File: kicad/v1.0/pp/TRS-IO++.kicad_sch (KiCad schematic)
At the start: 86 parts, among them J1 Conn_02x06_Odd_Even, J12 USB_B_Micro, J13 UART, J2 Interface Connector, J3 TRS-80 M3 Edge Connector, J5 Conn_02x06_Odd_Even, J6 Cassette Output, J7 HDMI, J8 Programmer, Q3 2N7002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

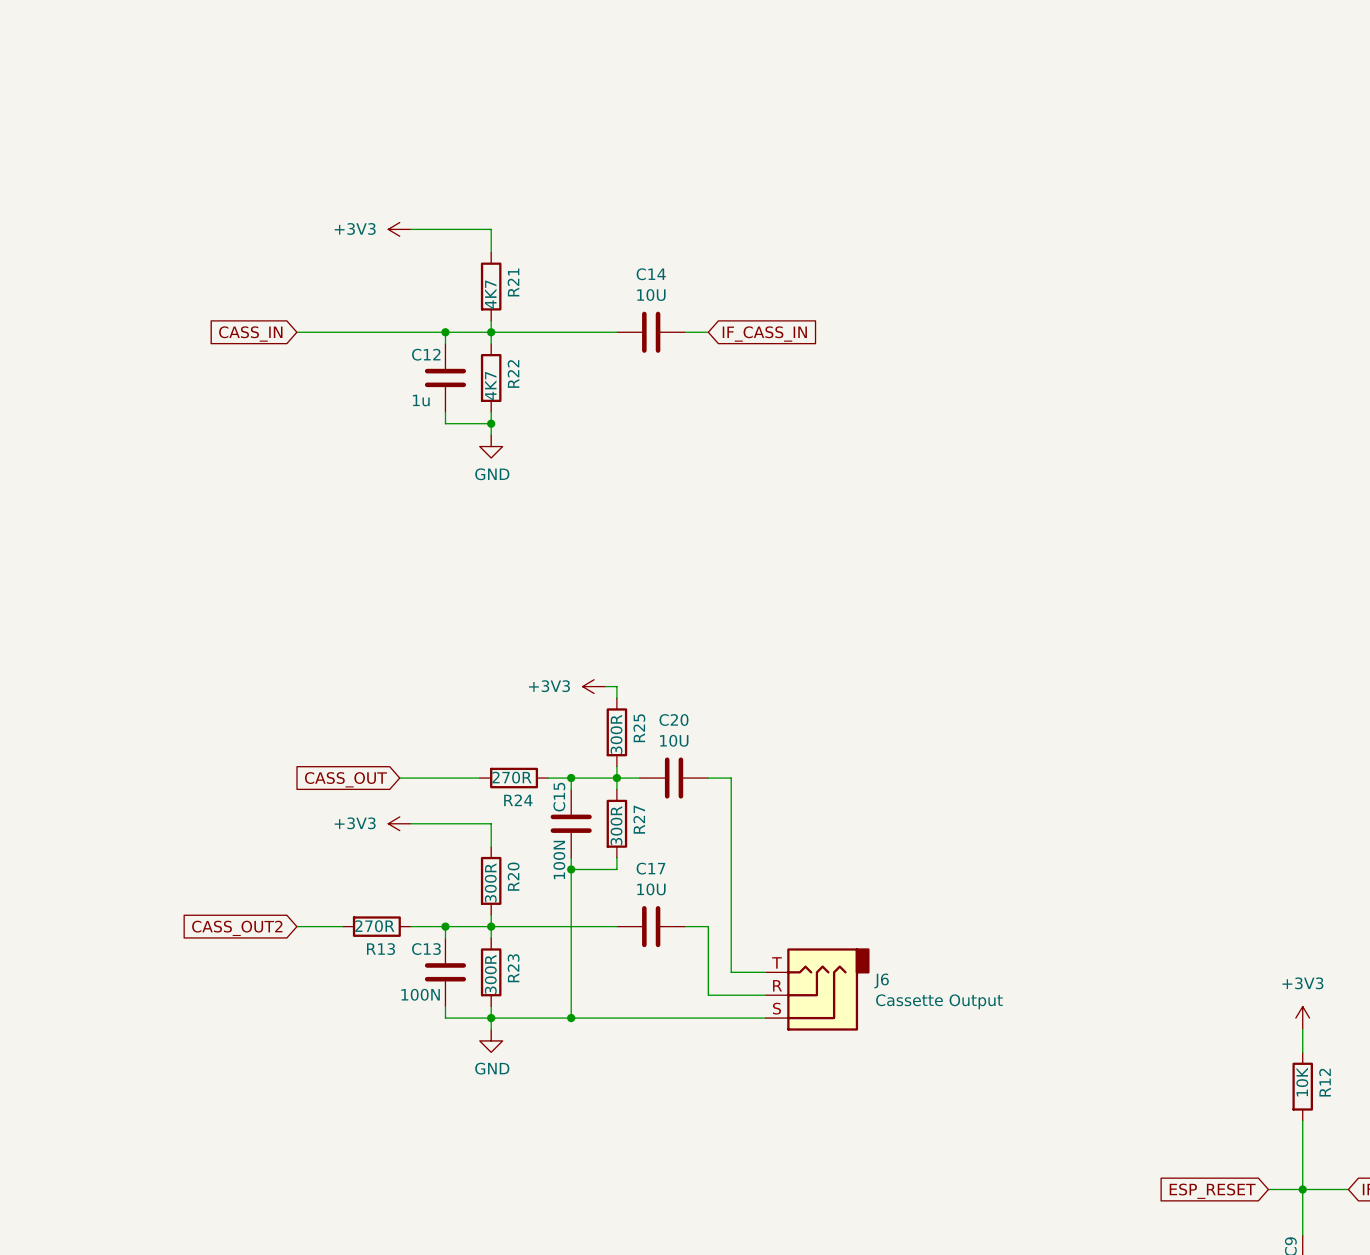
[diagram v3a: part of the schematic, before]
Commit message: Converted cassette to mono in/out.  Added audio amp.
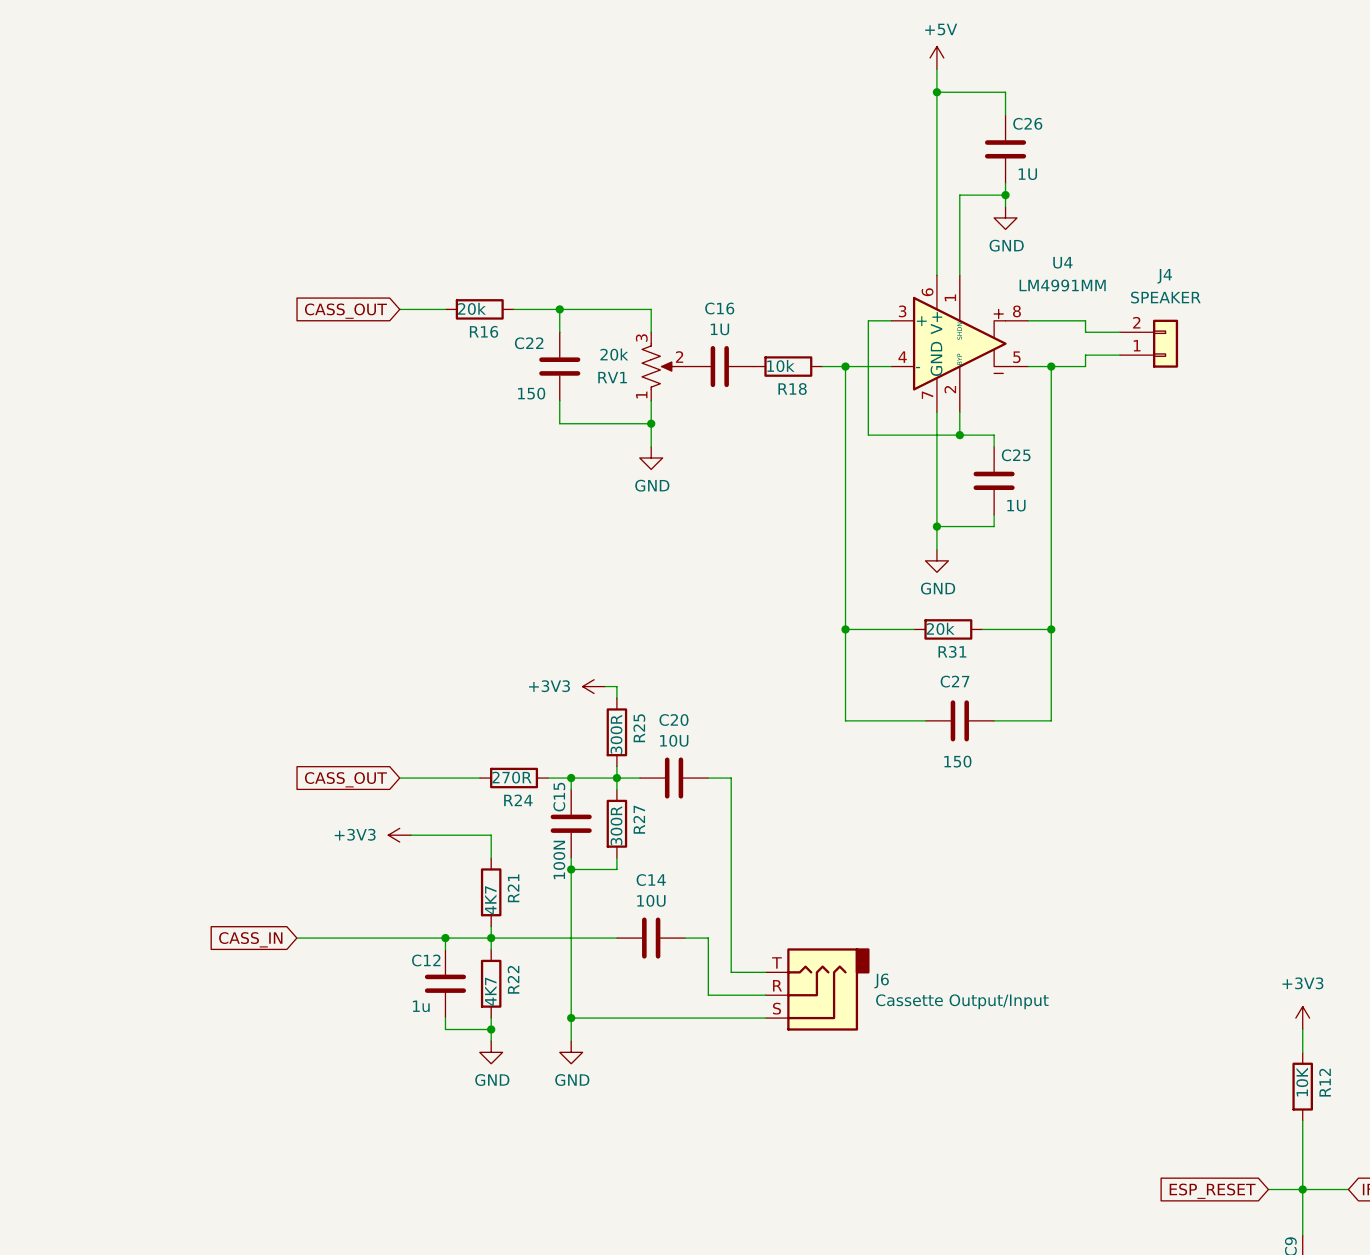
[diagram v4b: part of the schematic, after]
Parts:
- removed C13: 100N, Capacitor_SMD:C_0805_2012Metric_Pad1.18x1.45mm_HandSolder, symbol Device:C
- removed C17: 10U, Capacitor_SMD:C_1206_3216Metric_Pad1.33x1.80mm_HandSolder, symbol Device:C
- removed R13: 270R, Resistor_SMD:R_0805_2012Metric_Pad1.20x1.40mm_HandSolder, symbol Device:R
- removed R20, R23: 300R, Resistor_SMD:R_0805_2012Metric_Pad1.20x1.40mm_HandSolder, symbol Device:R
- added C16, C25, C26: 1U, Capacitor_SMD:C_0805_2012Metric_Pad1.18x1.45mm_HandSolder, symbol Device:C
- added C22, C27: 150, Capacitor_SMD:C_0805_2012Metric_Pad1.18x1.45mm_HandSolder, symbol Device:C
- added J4: SPEAKER, Connector_PinHeader_2.54mm:PinHeader_1x02_P2.54mm_Vertical, symbol Connector_Generic:Conn_01x02
- added R16, R31: 20k, Resistor_SMD:R_0805_2012Metric_Pad1.20x1.40mm_HandSolder, symbol Device:R
- added R18: 10k, Resistor_SMD:R_0805_2012Metric_Pad1.20x1.40mm_HandSolder, symbol Device:R
- added RV1: 20k, Potentiometer_SMD:Potentiometer_Bourns_TC33X_Vertical, symbol Device:R_Potentiometer_US
- added U4: LM4991MM, Package_SO:SOIC-8_3.9x4.9mm_P1.27mm, symbol Amplifier_Audio:LM4990MM
- J6: value Cassette Output -> Cassette Output/Input
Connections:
- net +5V: now also C26.1, U4.6 (V+)
- net CASS_OUT: now also R16.2
- net GND: now also C22.2, C25.2, C26.2, RV1.1, U4.1 (SHDN), U4.7 (GND)
- net IF_CASS_IN: no longer C14.1
- net at J6.R: now also C14.1
- new net: C25.1, U4.2 (BYP), U4.3 (+)
- new net: C27.2, R18.1, R31.2, U4.4 (-)
- new net: C27.1, J4.1 (Pin_1), R31.1, U4.5
- new net: J4.2 (Pin_2), U4.8
- new net: C16.2, RV1.2
- new net: C22.1, R16.1, RV1.3
- new net: C16.1, R18.2
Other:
- moved on the sheet: C12, C14, R21, R22

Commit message: First version of PCB (without HDMI)
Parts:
- removed D4, D5: LED, LED_SMD:LED_0805_2012Metric_Pad1.15x1.40mm_HandSolder, symbol Device:LED
- removed J12: USB_B_Micro, PocketTRS_Connectors:USBmicro-B, symbol MYLIB:USB_B_Micro
- removed J6: Cassette Output/Input, PocketTRS_Connectors:Jack_3.5mm_CUI_SJ1-3535NG_Horizontal_CircularHoles, symbol Connector:AudioJack3
- added J6: LED3, Connector_PinHeader_2.54mm:PinHeader_1x02_P2.54mm_Vertical, symbol Connector_Generic:Conn_01x02
- added J9: LED4, Connector_PinHeader_2.54mm:PinHeader_1x02_P2.54mm_Vertical, symbol Connector_Generic:Conn_01x02
- U4: LCSC (none) -> C2865568
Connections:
- net CD_SD: now also J2.15 (Pin_15); no longer J2.5 (Pin_5)
- net CS_SD: now also J2.14 (Pin_14); no longer J2.9 (Pin_9)
- net ESP_RESET: now also J2.9 (Pin_9); no longer J2.14 (Pin_14)
- net GND: now also J6.2 (Pin_2), J9.2 (Pin_2)
- net ID0: now also J2.10 (Pin_10); no longer J2.13 (Pin_13)
- net IF_BTN_TRSIO_STATUS: now also J2.12 (Pin_12); no longer J2.11 (Pin_11)
- net IF_CASS_IN: now also C14.1, J2.8 (Pin_8); no longer J2.12 (Pin_12)
- net IF_LED_BLUE: now also J2.5 (Pin_5); no longer J2.8 (Pin_8)
- net IF_LED_GREEN: now also J2.3 (Pin_3); no longer J2.6 (Pin_6)
- net IF_LED_RED: now also J2.7 (Pin_7); no longer J2.10 (Pin_10)
- net IF_RXD0: now also J2.6 (Pin_6); no longer J2.4 (Pin_4)
- net IF_SD_MISO: now also J2.11 (Pin_11); no longer J2.1 (Pin_1)
- net IF_SD_MOSI: now also J2.16 (Pin_16); no longer J2.7 (Pin_7)
- net IF_SD_SCK: now also J2.13 (Pin_13); no longer J2.3 (Pin_3)
- net IF_TXD0: now also J2.4 (Pin_4); no longer J2.2 (Pin_2)
- net IF_CASS_OUT: now reaches C20.1
- net IF_CASS_OUT: now also J2.2 (Pin_2)
- net at R39.2: now also J6.1 (Pin_1)
- net at R40.2: now also J9.1 (Pin_1)
- no-connect marks 11 -> 8
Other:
- moved on the sheet: D2, D3, R37, R38, R39, R40

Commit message: Converted HDMI connector to SMD.
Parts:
- J7: footprint Connector_PinHeader_1.27mm:PinHeader_2x05_P1.27mm_Vertical -> Connector_PinHeader_1.27mm:PinHeader_2x05_P1.27mm_Vertical_SMD
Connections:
- net CK+: now also J7.1 (Pin_1); no longer J7.7 (Pin_7)
- net CK-: now also J7.2 (Pin_2); no longer J7.8 (Pin_8)
- net D0+: now also J7.3 (Pin_3); no longer J7.5 (Pin_5)
- net D0-: now also J7.4 (Pin_4); no longer J7.6 (Pin_6)
- net D1+: now also J7.5 (Pin_5); no longer J7.3 (Pin_3)
- net D1-: now also J7.6 (Pin_6); no longer J7.4 (Pin_4)
- net D2+: now also J7.7 (Pin_7); no longer J7.1 (Pin_1)
- net D2-: now also J7.8 (Pin_8); no longer J7.2 (Pin_2)
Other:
- moved on the sheet: J7
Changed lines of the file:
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@@
 	)
 	(junction
+		(at 248.92 91.44)
+		(diameter 0)
+		(color 0 0 0 0)
+	)
+	(junction
 		(at 441.96 369.57)
 		(diameter 0)
@@
 	)
 	(junction
-		(at 248.92 91.44)
-		(diameter 0)
-		(color 0 0 0 0)
-	)
-	(junction
 		(at 238.76 349.25)
 		(diameter 0)
@@
 	(wire
 		(pts
-			(xy 279.4 83.82) (xy 271.78 83.82)
-		)
-		(stroke
-			(width 0)
-			(type default)
-		)
-	)
-	(wire
-		(pts
 			(xy 142.24 373.38) (xy 139.7 373.38)
 		)
@@
 	(wire
 		(pts
+			(xy 271.78 83.82) (xy 279.4 83.82)
+		)
+		(stroke
+			(width 0)
+			(type default)
+		)
+	)
+	(wire
+		(pts
 			(xy 276.86 48.26) (xy 280.67 48.26)
 		)
@@
 	(wire
 		(pts
-			(xy 299.72 88.9) (xy 292.1 88.9)
+			(xy 373.38 360.68) (xy 378.46 360.68)
 		)
 		(stroke
@@
 	(wire
 		(pts
-			(xy 373.38 360.68) (xy 378.46 360.68)
+			(xy 425.45 58.42) (xy 425.45 87.63)
 		)
 		(stroke
@@
 	(wire
 		(pts
-			(xy 425.45 58.42) (xy 425.45 87.63)
+			(xy 97.79 328.93) (xy 88.9 328.93)
 		)
 		(stroke
@@
 	(wire
 		(pts
-			(xy 97.79 328.93) (xy 88.9 328.93)
+			(xy 53.34 248.92) (xy 53.34 251.46)
 		)
 		(stroke
@@
 	(wire
 		(pts
-			(xy 53.34 248.92) (xy 53.34 251.46)
+			(xy 248.92 91.44) (xy 279.4 91.44)
 		)
 		(stroke
@@
 	(wire
 		(pts
+			(xy 276.86 81.28) (xy 279.4 81.28)
+		)
+		(stroke
+			(width 0)
+			(type default)
+		)
+	)
+	(wire
+		(pts
 			(xy 496.57 105.41) (xy 496.57 107.95)
 		)
@@
 	(wire
 		(pts
-			(xy 281.94 354.33) (xy 284.48 354.33)
+			(xy 292.1 88.9) (xy 299.72 88.9)
 		)
 		(stroke
@@
 	(wire
 		(pts
-			(xy 88.9 308.61) (xy 91.44 308.61)
+			(xy 281.94 354.33) (xy 284.48 354.33)
 		)
 		(stroke
@@
 	(wire
 		(pts
-			(xy 91.44 339.09) (xy 91.44 346.71)
+			(xy 88.9 308.61) (xy 91.44 308.61)
 		)
 		(stroke
@@
 	(wire
 		(pts
-			(xy 57.15 203.2) (xy 53.34 203.2)
+			(xy 91.44 339.09) (xy 91.44 346.71)
 		)
 		(stroke
@@
 	(wire
 		(pts
-			(xy 236.22 35.56) (xy 236.22 39.37)
+			(xy 57.15 203.2) (xy 53.34 203.2)
 		)
 		(stroke
@@
 	(wire
 		(pts
-			(xy 284.48 311.15) (xy 284.48 318.77)
+			(xy 236.22 35.56) (xy 236.22 39.37)
 		)
 		(stroke
@@
 	(wire
 		(pts
-			(xy 43.18 372.11) (xy 48.26 372.11)
+			(xy 284.48 311.15) (xy 284.48 318.77)
 		)
 		(stroke
@@
 	(wire
 		(pts
-			(xy 182.88 325.12) (xy 187.96 325.12)
+			(xy 43.18 372.11) (xy 48.26 372.11)
 		)
 		(stroke
@@
 	(wire
 		(pts
-			(xy 292.1 93.98) (xy 294.64 93.98)
+			(xy 182.88 325.12) (xy 187.96 325.12)
 		)
 		(stroke
@@
 	(wire
 		(pts
-			(xy 279.4 86.36) (xy 269.24 86.36)
-		)
-		(stroke
-			(width 0)
-			(type default)
-		)
-	)
-	(wire
-		(pts
 			(xy 53.34 220.98) (xy 53.34 223.52)
 		)
@@
 	(wire
 		(pts
-			(xy 299.72 86.36) (xy 292.1 86.36)
-		)
-		(stroke
-			(width 0)
-			(type default)
-		)
-	)
-	(wire
-		(pts
 			(xy 185.42 381) (xy 185.42 386.08)
 		)
@@
 	(wire
 		(pts
+			(xy 292.1 86.36) (xy 299.72 86.36)
+		)
+		(stroke
+			(width 0)
+			(type default)
+		)
+	)
+	(wire
+		(pts
 			(xy 137.16 347.98) (xy 142.24 347.98)
 		)
@@
 	(wire
 		(pts
-			(xy 292.1 91.44) (xy 297.18 91.44)
-		)
-		(stroke
-			(width 0)
-			(type default)
-		)
-	)
-	(wire
-		(pts
 			(xy 88.9 62.23) (xy 96.52 62.23)
 		)
@@
 	(wire
 		(pts
-			(xy 248.92 91.44) (xy 279.4 91.44)
-		)
-		(stroke
-			(width 0)
-			(type default)
-		)
-	)
-	(wire
-		(pts
 			(xy 358.14 250.19) (xy 358.14 255.27)
 		)
@@
 	(wire
 		(pts
+			(xy 269.24 86.36) (xy 279.4 86.36)
+		)
+		(stroke
+			(width 0)
+			(type default)
+		)
+	)
+	(wire
+		(pts
 			(xy 177.8 148.59) (xy 185.42 148.59)
 		)
@@
 	(wire
 		(pts
+			(xy 294.64 81.28) (xy 294.64 105.41)
+		)
+		(stroke
+			(width 0)
+			(type default)
+		)
+	)
+	(wire
+		(pts
 			(xy 505.46 170.18) (xy 514.35 170.18)
 		)
@@
 	(wire
 		(pts
+			(xy 266.7 88.9) (xy 279.4 88.9)
+		)
+		(stroke
+			(width 0)
+			(type default)
+		)
+	)
+	(wire
+		(pts
 			(xy 229.87 35.56) (xy 229.87 39.37)
 		)
@@
 	(wire
 		(pts
-			(xy 279.4 88.9) (xy 266.7 88.9)
-		)
-		(stroke
-			(width 0)
-			(type default)
-		)
-	)
-	(wire
-		(pts
 			(xy 254 160.02) (xy 259.08 160.02)
 		)
@@
 	(wire
 		(pts
-			(xy 294.64 93.98) (xy 294.64 105.41)
-		)
-		(stroke
-			(width 0)
-			(type default)
-		)
-	)
-	(wire
-		(pts
 			(xy 88.9 334.01) (xy 93.98 334.01)
 		)
@@
 	(wire
 		(pts
+			(xy 292.1 81.28) (xy 294.64 81.28)
+		)
+		(stroke
+			(width 0)
+			(type default)
+		)
+	)
+	(wire
+		(pts
 			(xy 393.7 125.73) (xy 389.89 125.73)
 		)
@@
 	(wire
 		(pts
-			(xy 276.86 93.98) (xy 279.4 93.98)
+			(xy 284.48 341.63) (xy 284.48 346.71)
 		)
 		(stroke
@@
 	(wire
 		(pts
-			(xy 284.48 341.63) (xy 284.48 346.71)
+			(xy 97.79 326.39) (xy 97.79 328.93)
 		)
 		(stroke
@@
 	(wire
 		(pts
-			(xy 97.79 326.39) (xy 97.79 328.93)
+			(xy 260.35 217.17) (xy 265.43 217.17)
 		)
 		(stroke
@@
 	(wire
 		(pts
-			(xy 260.35 217.17) (xy 265.43 217.17)
+			(xy 69.85 205.74) (xy 74.93 205.74)
 		)
 		(stroke
@@
 	(wire
 		(pts
-			(xy 69.85 205.74) (xy 74.93 205.74)
+			(xy 292.1 83.82) (xy 297.18 83.82)
 		)
 		(stroke
@@
 	(wire
 		(pts
-			(xy 292.1 83.82) (xy 297.18 83.82)
+			(xy 292.1 91.44) (xy 297.18 91.44)
 		)
 		(stroke
@@
 	(wire
 		(pts
-			(xy 276.86 48.26) (xy 276.86 93.98)
+			(xy 276.86 48.26) (xy 276.86 81.28)
 		)
 		(stroke
@@
 	(symbol
 		(lib_id "Connector_Generic:Conn_02x05_Odd_Even")
-		(at 284.48 88.9 0)
+		(at 284.48 86.36 0)
+		(mirror x)
 		(unit 1)
 		(exclude_from_sim no)
@@
 		(on_board yes)
 		(dnp no)
-		(fields_autoplaced yes)
 		(property "Reference" "J7"
-			(at 285.75 77.47 0)
+			(at 285.75 97.79 0)
 			(effects
 				(font
@@
 		)
 		(property "Value" "HDMI"
-			(at 285.75 80.01 0)
+			(at 285.75 95.25 0)
 			(effects
 				(font
@@
 			)
 		)
-		(property "Footprint" "Connector_PinHeader_1.27mm:PinHeader_2x05_P1.27mm_Vertical"
-			(at 284.48 88.9 0)
+		(property "Footprint" "Connector_PinHeader_1.27mm:PinHeader_2x05_P1.27mm_Vertical_SMD"
+			(at 284.48 86.36 0)
 			(effects
 				(font
@@
 		)
 		(property "Datasheet" "~"
-			(at 284.48 88.9 0)
+			(at 284.48 86.36 0)
 			(effects
 				(font
@@
 		)
 		(property "Description" "Generic connector, double row, 02x05, odd/even pin numbering scheme (row 1 odd numbers, row 2 even numbers), script generated (kicad-library-utils/schlib/autogen/connector/)"
-			(at 284.48 88.9 0)
+			(at 284.48 86.36 0)
 			(effects
 				(font

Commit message: First version of MiniTRS PCB
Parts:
- J2: footprint Connector_PinHeader_2.54mm:PinHeader_2x10_P2.54mm_Vertical -> Connector_PinHeader_1.27mm:PinHeader_2x10_P1.27mm_Vertical
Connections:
- net GND: now also J2.2 (Pin_2)
- net IF_CASS_OUT: now also J2.1 (Pin_1); no longer J2.2 (Pin_2)
- net IF_LED_GREEN: now also J2.7 (Pin_7); no longer J2.3 (Pin_3)
- net IF_LED_RED: now also J2.3 (Pin_3); no longer J2.7 (Pin_7)
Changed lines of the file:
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@@
 	(wire
 		(pts
-			(xy 66.04 142.24) (xy 53.34 142.24)
-		)
-		(stroke
-			(width 0)
-			(type default)
-		)
-	)
-	(wire
-		(pts
 			(xy 91.44 389.89) (xy 91.44 401.32)
 		)
@@
 	(wire
 		(pts
-			(xy 78.74 142.24) (xy 91.44 142.24)
+			(xy 78.74 142.24) (xy 123.19 142.24)
 		)
 		(stroke
@@
 	(wire
 		(pts
+			(xy 53.34 142.24) (xy 66.04 142.24)
+		)
+		(stroke
+			(width 0)
+			(type default)
+		)
+	)
+	(wire
+		(pts
 			(xy 292.1 83.82) (xy 297.18 83.82)
 		)
@@
 		)
 	)
+	(wire
+		(pts
+			(xy 123.19 142.24) (xy 123.19 147.32)
+		)
+		(stroke
+			(width 0)
+			(type default)
+		)
+	)
 	(label "HDMI_TX2+"
 		(at 177.8 53.34 0)
@@
 	(global_label "IF_CASS_OUT"
 		(shape input)
-		(at 91.44 142.24 0)
+		(at 53.34 142.24 180)
 		(fields_autoplaced yes)
 		(effects
@@
 				(size 1.27 1.27)
 			)
-			(justify left)
+			(justify right)
 		)
 		(property "Intersheetrefs" "${INTERSHEET_REFS}"
-			(at 106.46 142.24 0)
+			(at 38.32 142.24 0)
 			(effects
 				(font
 					(size 1.27 1.27)
 				)
-				(justify left)
+				(justify right)
 				(hide yes)
 			)
@@
 	(global_label "IF_LED_RED"
 		(shape input)
-		(at 53.34 149.86 180)
+		(at 53.34 144.78 180)
 		(fields_autoplaced yes)
 		(effects
@@
 		)
 		(property "Intersheetrefs" "${INTERSHEET_REFS}"
-			(at 39.5901 149.86 0)
+			(at 39.5901 144.78 0)
 			(effects
 				(font
@@
 	(global_label "IF_LED_GREEN"
 		(shape input)
-		(at 53.34 144.78 180)
+		(at 53.34 149.86 180)
 		(fields_autoplaced yes)
 		(effects
@@
 		)
 		(property "Intersheetrefs" "${INTERSHEET_REFS}"
-			(at 37.1106 144.78 0)
+			(at 37.1106 149.86 0)
 			(effects
 				(font
@@
 	)
 	(symbol
+		(lib_name "GND_4")
+		(lib_id "power:GND")
+		(at 123.19 147.32 0)
+		(unit 1)
+		(exclude_from_sim no)
+		(in_bom yes)
+		(on_board yes)
+		(dnp no)
+		(fields_autoplaced yes)
+		(property "Reference" "#PWR036"
+			(at 123.19 153.67 0)
+			(effects
+				(font
+					(size 1.27 1.27)
+				)
+				(hide yes)
+			)
+		)
+		(property "Value" "GND"
+			(at 123.19 152.4 0)
+			(effects
+				(font
+					(size 1.27 1.27)
+				)
+			)
+		)
+		(property "Footprint" ""
+			(at 123.19 147.32 0)
+			(effects
+				(font
+					(size 1.27 1.27)
+				)
+				(hide yes)
+			)
+		)
+		(property "Datasheet" ""
+			(at 123.19 147.32 0)
+			(effects
+				(font
+					(size 1.27 1.27)
+				)
+				(hide yes)
+			)
+		)
+		(property "Description" "Power symbol creates a global label with name \"GND\" , ground"
+			(at 123.19 147.32 0)
+			(effects
+				(font
+					(size 1.27 1.27)
+				)
+				(hide yes)
+			)
+		)
+		(pin "1"
+		)
+		(instances
+			(project "TRS-IO++"
+				(path "/cbbd5873-4a60-4f28-a36a-d78c2a00c151"
+					(reference "#PWR036")
+					(unit 1)
+				)
+			)
+		)
+	)
+	(symbol
 		(lib_id "Device:R")
 		(at 541.02 96.52 0)
@@
 			)
 		)
-		(property "Footprint" "Connector_PinHeader_2.54mm:PinHeader_2x10_P2.54mm_Vertical"
+		(property "Footprint" "Connector_PinHeader_1.27mm:PinHeader_2x10_P1.27mm_Vertical"
 			(at 71.12 152.4 0)
 			(effects

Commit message: Changed J4 connector for speaker
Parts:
- C22, C27: value 150 -> 150pF
- J2: LCSC (none) -> C3324132
- J4: footprint Connector_PinHeader_2.54mm:PinHeader_1x02_P2.54mm_Vertical -> Connector_PinHeader_2.54mm:PinHeader_1x02_P2.54mm_Horizontal; LCSC C2937625 -> C492410
- J6, J9: LCSC (none) -> C225477
- J7: LCSC (none) -> C598540
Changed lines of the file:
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@@
 			)
 		)
+		(property "LCSC" "C598540"
+			(at 284.48 86.36 0)
+			(effects
+				(font
+					(size 1.27 1.27)
+				)
+				(hide yes)
+			)
+		)
 		(pin "3"
 		)
@@
 			)
 		)
-		(property "Value" "150"
+		(property "Value" "150pF"
 			(at 415.036 102.362 90)
 			(effects
@@
 			)
 		)
+		(property "LCSC" "C3324132"
+			(at 71.12 152.4 0)
+			(effects
+				(font
+					(size 1.27 1.27)
+				)
+				(hide yes)
+			)
+		)
 		(pin "2"
 		)
@@
 			)
 		)
-		(property "Footprint" "Connector_PinHeader_2.54mm:PinHeader_1x02_P2.54mm_Vertical"
+		(property "Footprint" "Connector_PinHeader_2.54mm:PinHeader_1x02_P2.54mm_Horizontal"
 			(at 438.15 57.15 0)
 			(effects
@@
 			)
 		)
-		(property "LCSC" "C2937625"
+		(property "LCSC" "C492410"
 			(at 438.15 57.15 0)
 			(effects
@@
 			)
 		)
-		(property "Value" "150"
+		(property "Value" "150pF"
 			(at 366.014 61.468 0)
 			(effects
@@
 			)
 		)
+		(property "LCSC" "C225477"
+			(at 186.69 227.33 0)
+			(effects
+				(font
+					(size 1.27 1.27)
+				)
+				(hide yes)
+			)
+		)
 		(pin "2"
 		)
@@
 			(at 186.69 209.55 0)
 			(effects
+				(font
+					(size 1.27 1.27)
+				)
+				(hide yes)
+			)
+		)
+		(property "LCSC" "C225477"
+			(at 186.69 209.55 0)
+			(effects
